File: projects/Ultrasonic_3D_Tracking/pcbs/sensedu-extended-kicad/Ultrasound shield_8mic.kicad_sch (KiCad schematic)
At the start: 26 parts, among them J1 Power, J10 Barrel_Jack_Switch, J13 Conn_02x01, J14 Conn_02x01, J15 Conn_02x01, J18 Conn_03x01, J2 PWM, J3 Analog, J4 PWM, J5 Analog, J6 Communication, J7 Digital, U12 TLS850C2TE_V33, U13 NCP1117-2.5_SOT223

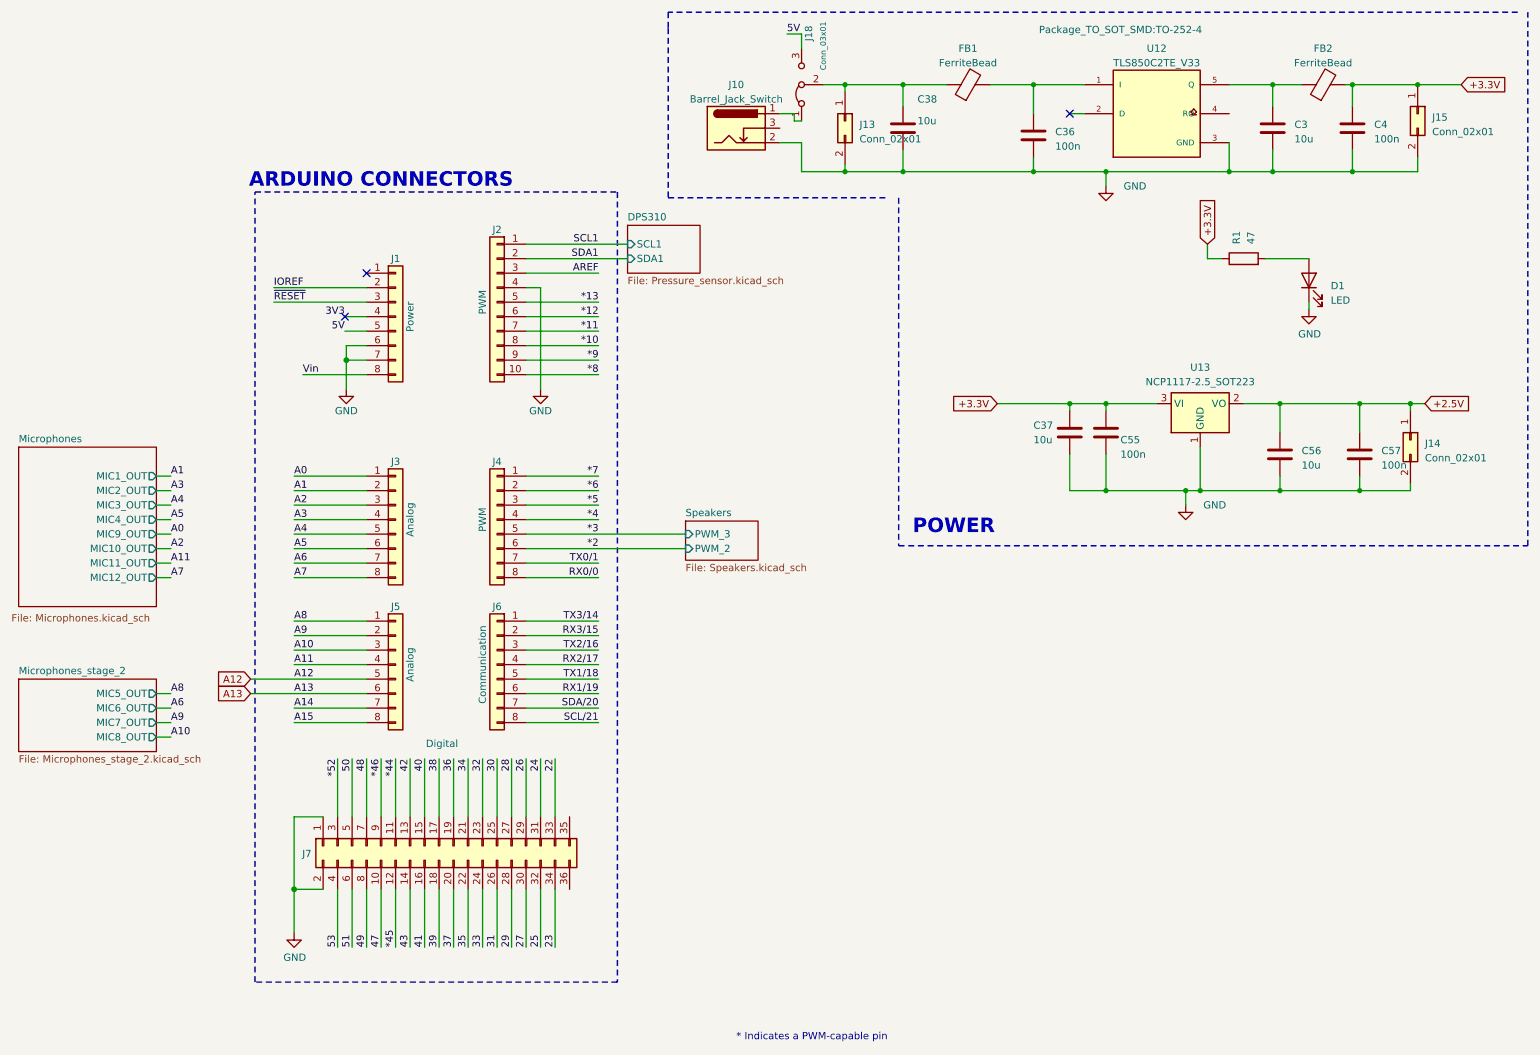
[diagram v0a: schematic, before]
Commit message: Fix: Cleaned schematic
- project is not correctly set up, so cannot be ordered without further
   work
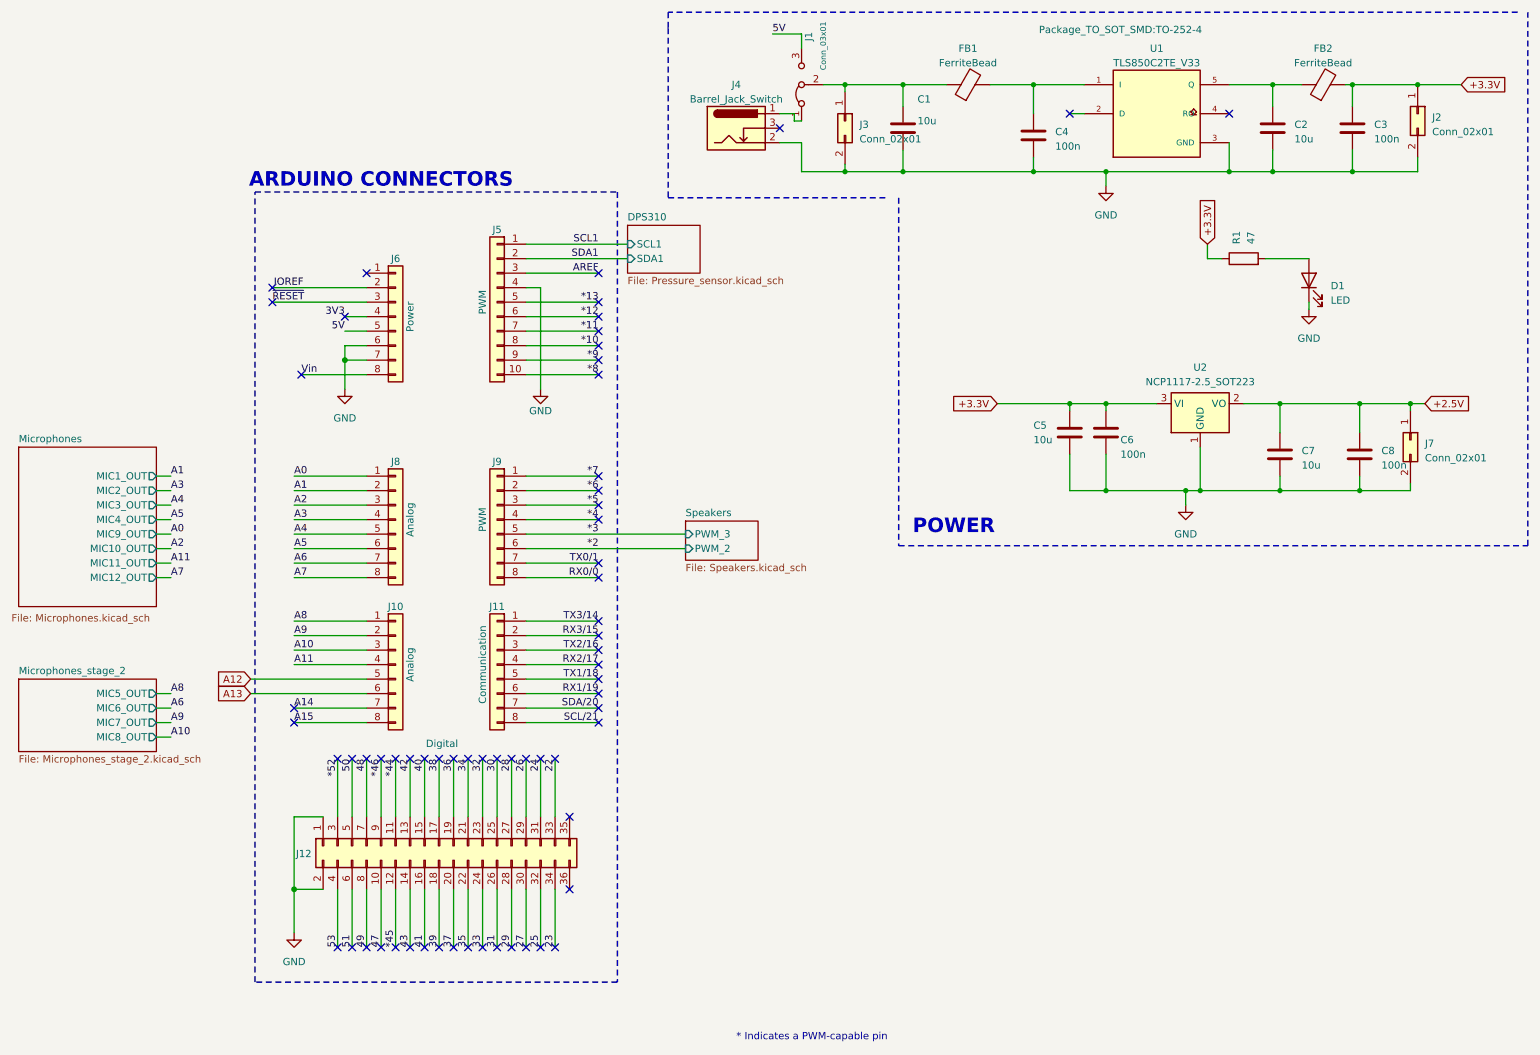
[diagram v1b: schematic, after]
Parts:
- renumbered C38 to C1, C3 to C2, C4 to C3, C36 to C4, C37 to C5, C55 to C6, C56 to C7, C57 to C8, J18 to J1, J5 to J10, J6 to J11, J7 to J12, J15 to J2, J13 to J3, J10 to J4, J2 to J5, J1 to J6, J14 to J7, J3 to J8, J4 to J9, U12 to U1, U13 to U2
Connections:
- no-connect marks 3 -> 65
